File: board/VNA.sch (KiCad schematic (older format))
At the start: 75 parts, among them J1 Conn_02x05_Odd_Even, J10 Conn_01x01, J11 Conn_01x01, J12 Conn_01x01, J13 Barrel_Jack, J15 Conn_02x05_Odd_Even, J17 Conn_01x04, J18 Conn_01x01, J19 Conn_01x01, J2 Conn_Coaxial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

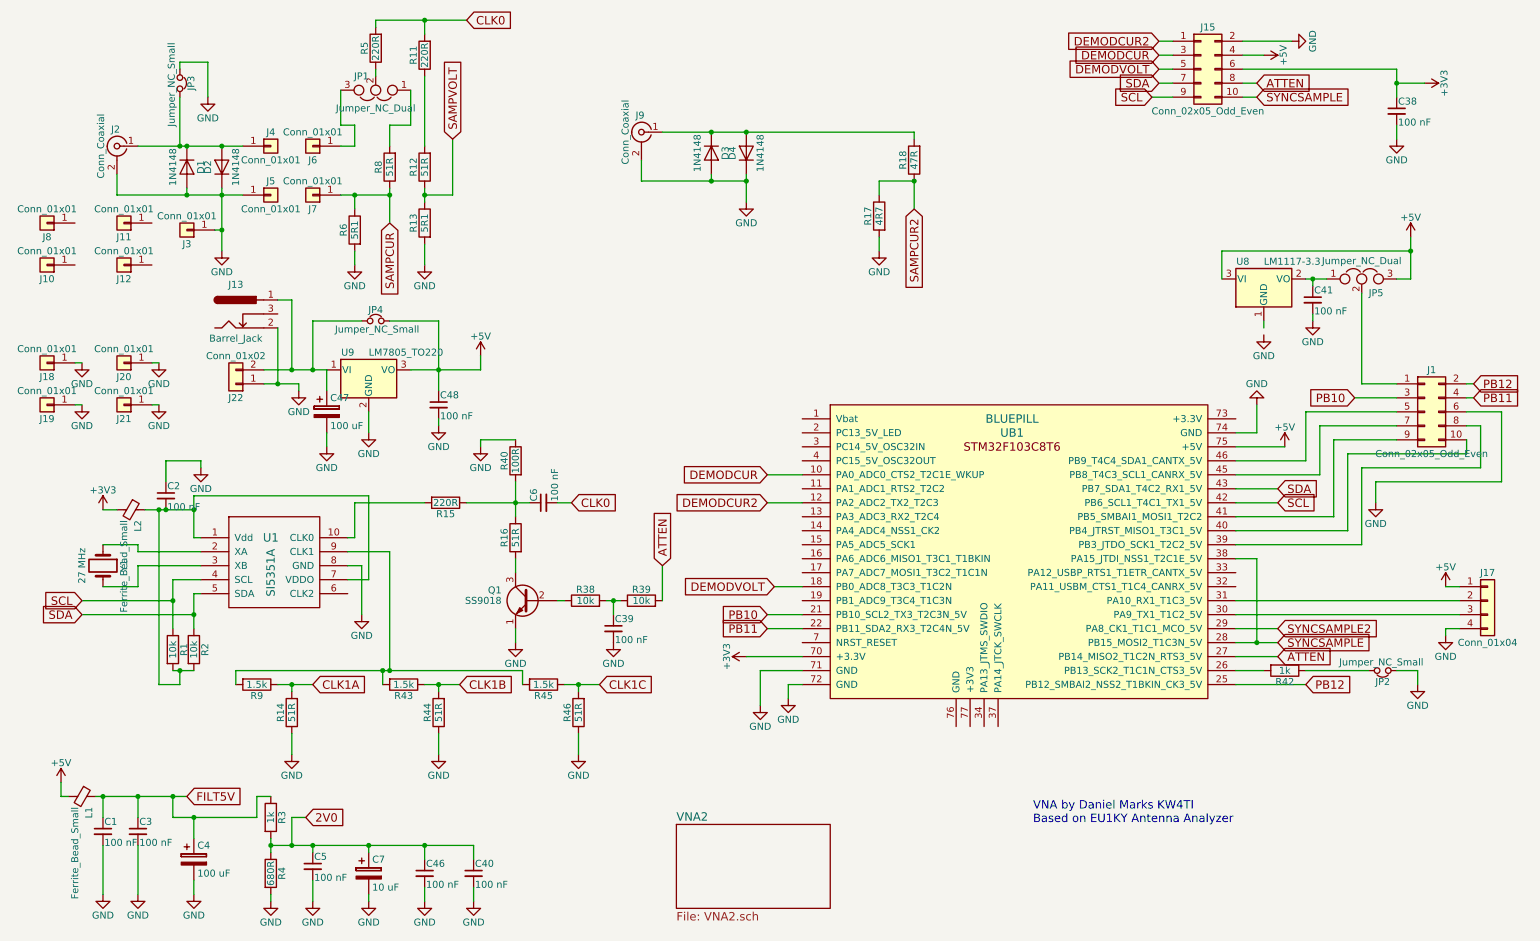
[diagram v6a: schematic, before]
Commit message: Added extra outputs to connector, changed display off pin
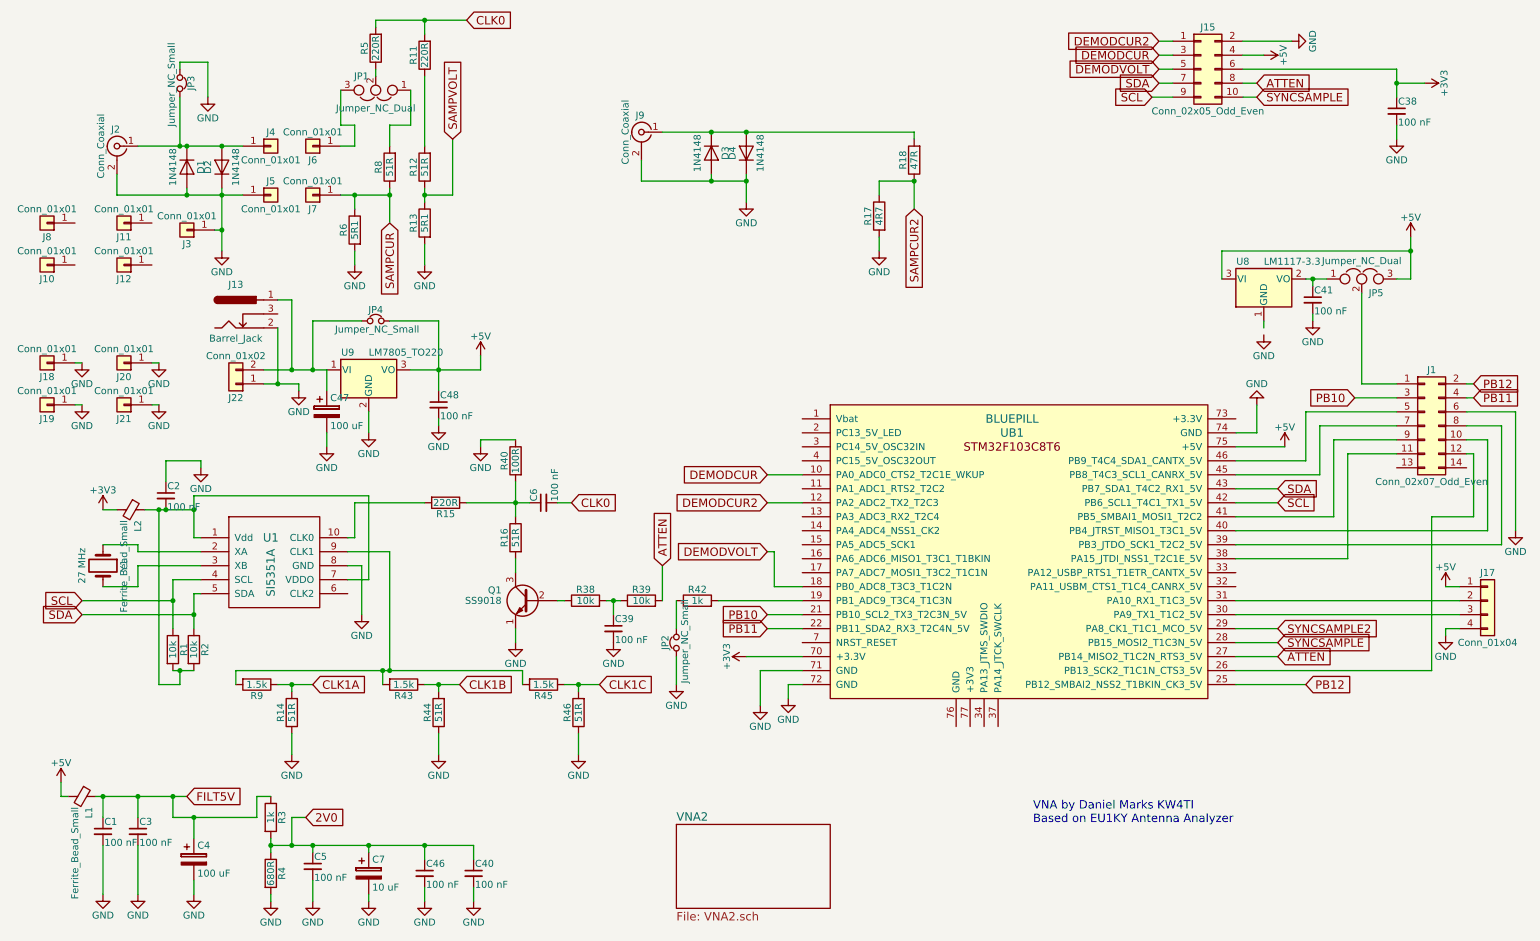
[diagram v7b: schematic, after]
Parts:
- removed J1: Conn_02x05_Odd_Even, Pin_Headers:Pin_Header_Straight_2x05_Pitch2.54mm, symbol Conn_02x05_Odd_Even
- added J1: Conn_02x07_Odd_Even, Pin_Headers:Pin_Header_Straight_2x07_Pitch2.54mm, symbol Conn_02x07_Odd_Even
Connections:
- net GND: now also J1.6 (Pin_6)
- net PB10: now also J1.3 (Pin_3)
- net PB11: now also J1.4 (Pin_4)
- net PB12: now also J1.2 (Pin_2)
- net SYNCSAMPLE: no longer UB1.38 (PA15_JTDI_NSS1_T2C1E_5V)
- net at UB1.19 (PB1_ADC9_T3C4_T1C3N): now also R42.2
- net at UB1.26 (PB13_SCK2_T1C1N_CTS3_5V): now also J1.12 (Pin_12); no longer R42.2
- net at UB1.39 (PB3_JTDO_SCK1_T2C2_5V): now also J1.8 (Pin_8)
- net at UB1.40 (PB4_JTRST_MISO1_T3C1_5V): now also J1.10 (Pin_10)
- net at UB1.41 (PB5_SMBAI1_MOSI1_T2C2): now also J1.9 (Pin_9)
- net at UB1.45 (PB8_T4C3_SCL1_CANRX_5V): now also J1.7 (Pin_7)
- net at UB1.46 (PB9_T4C4_SDA1_CANTX_5V): now also J1.5 (Pin_5)
- net at JP5.2: now also J1.1 (Pin_1)
- new net: J1.11 (Pin_11), UB1.38 (PA15_JTDI_NSS1_T2C1E_5V)
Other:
- moved on the sheet: JP2, R42

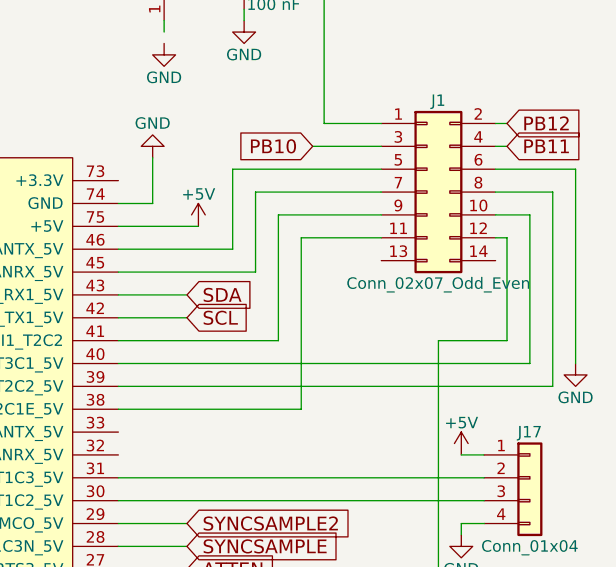
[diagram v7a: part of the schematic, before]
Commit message: Added vacuum holes to fixture
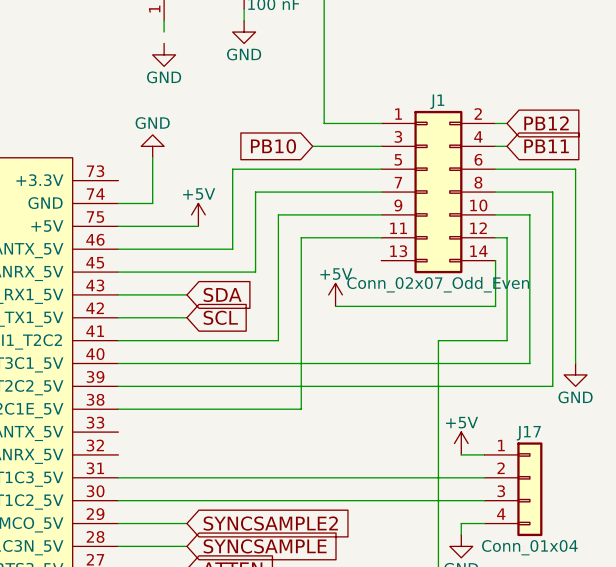
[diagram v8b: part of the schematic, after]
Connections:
- net +5V: now also J1.14 (Pin_14)
